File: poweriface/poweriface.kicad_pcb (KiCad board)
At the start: 2 copper layers, 25 x 42.5 mm, 21 parts, among them J1 Power Board, J2 CAN In, J3 CAN Out, J4 AVR-ISP-6, U1 ATmega32M1-AU, U2 MCP2551-I-SN, Y1 16MHz

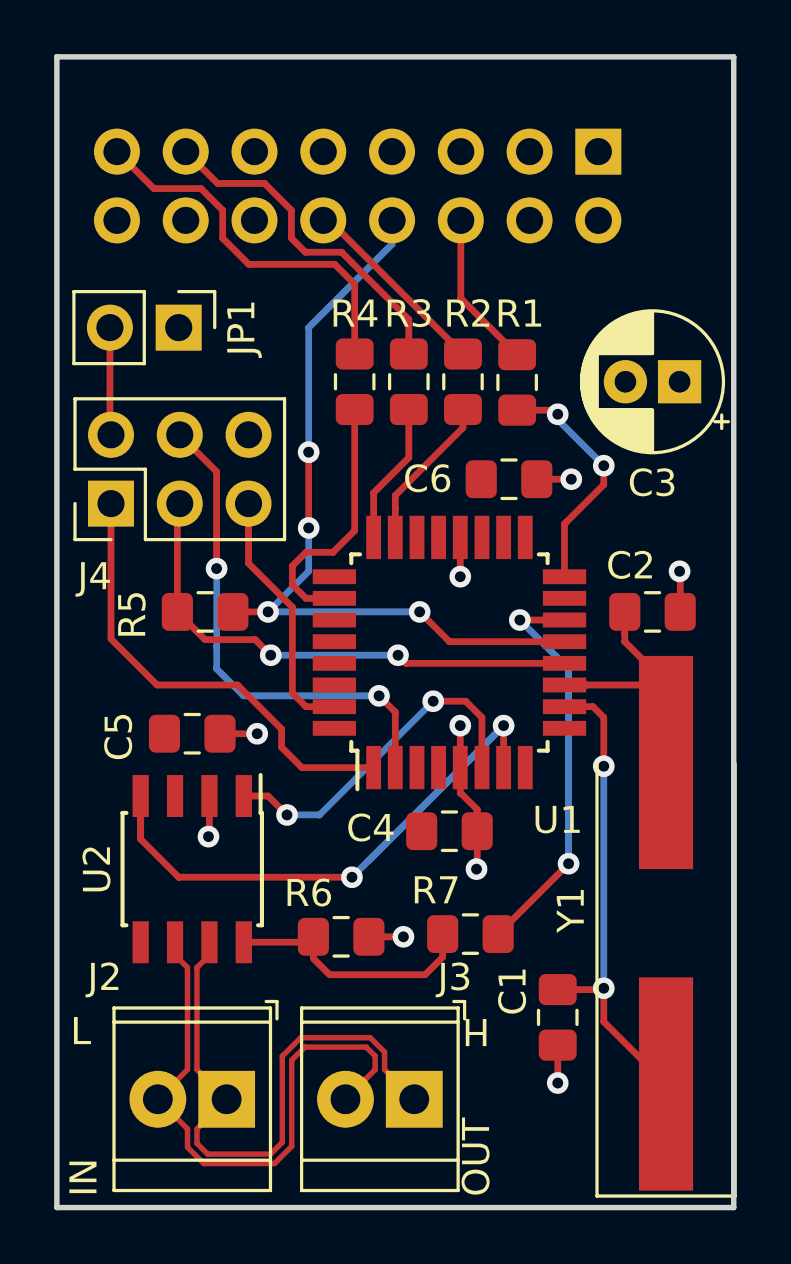
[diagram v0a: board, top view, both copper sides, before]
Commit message: Replaced crystal footprint with less wasteful one
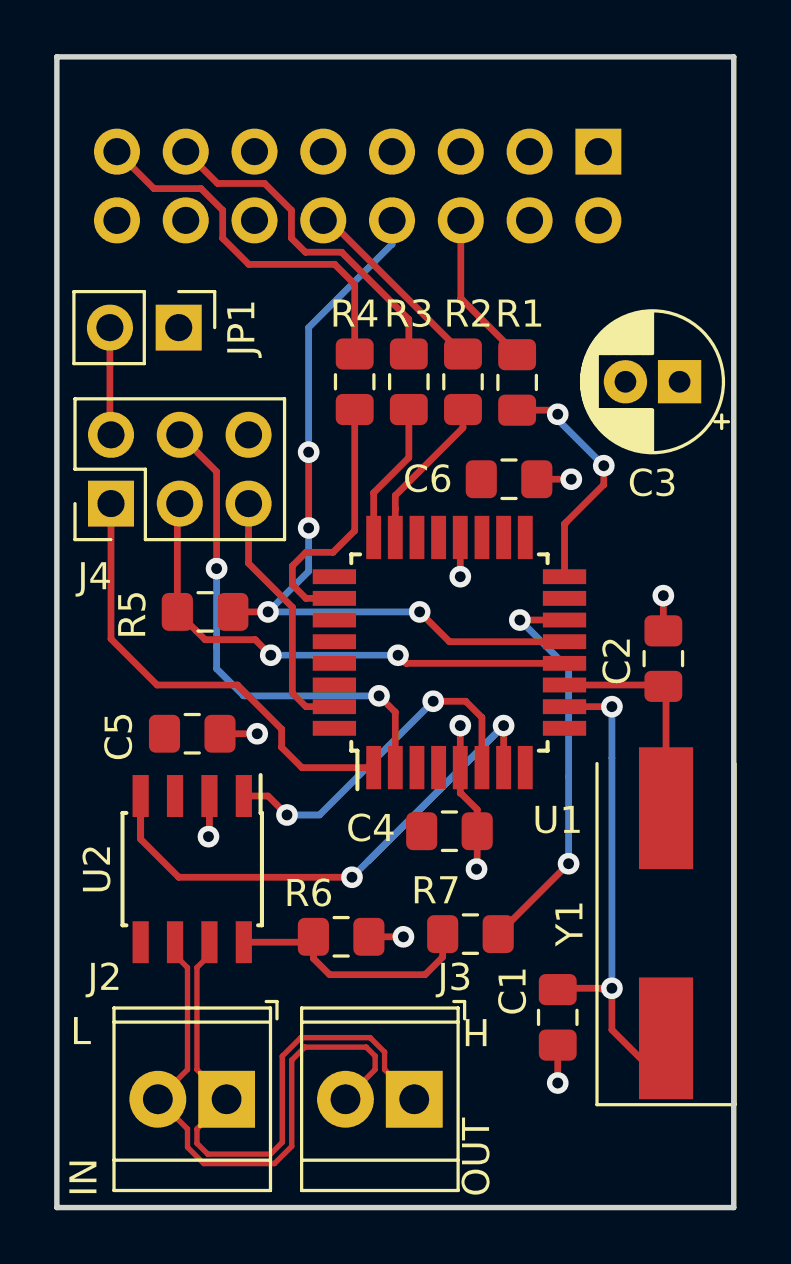
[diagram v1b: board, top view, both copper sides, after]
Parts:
- Y1: footprint Crystal:Crystal_SMD_HC49-SD_HandSoldering -> Crystal:Crystal_SMD_HC49-SD
- moved C2 1.77 mm to (192.4, 98.7), turned to 270 degrees
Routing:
- net Net-(C2-Pad2): track 12.6 -> 8.21 mm
- net Net-(C1-Pad2): track 17.8 -> 18.6 mm

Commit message: Added ground terminals
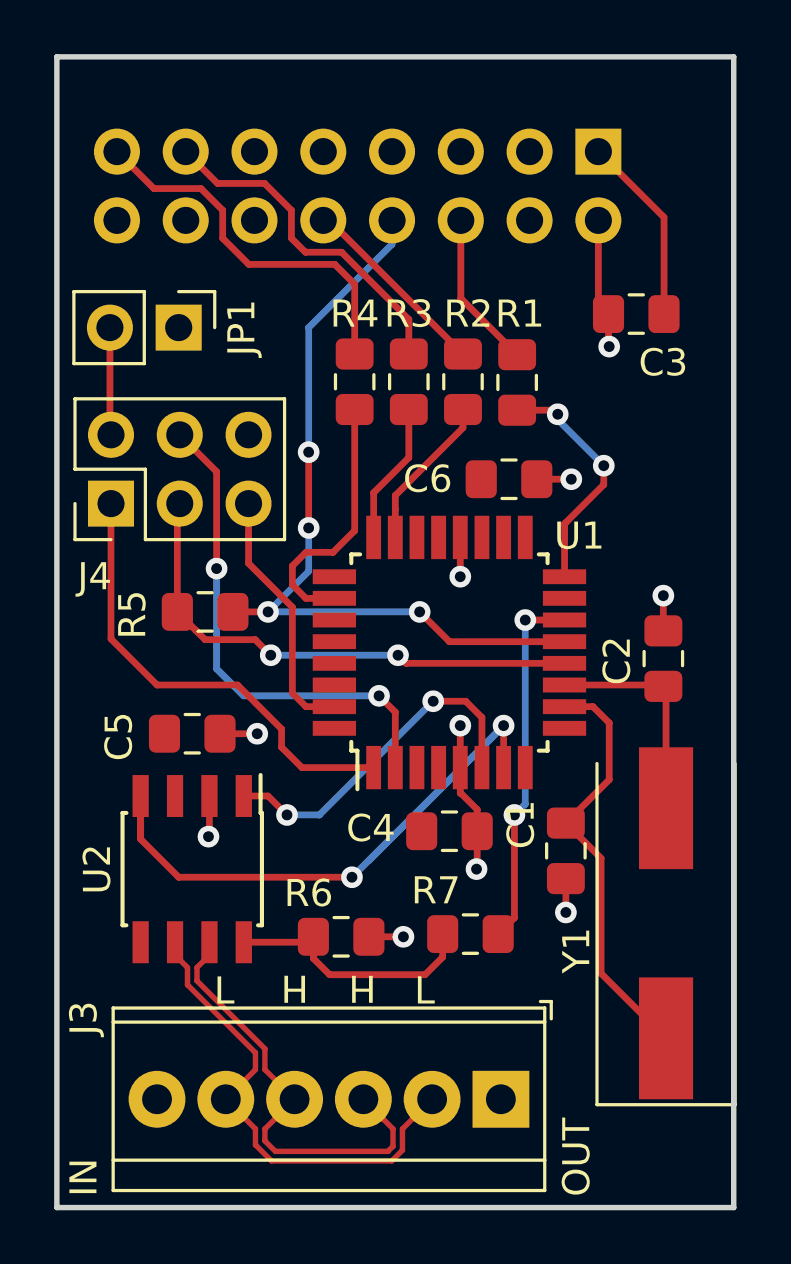
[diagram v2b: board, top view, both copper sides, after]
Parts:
- removed J2: CAN In, TerminalBlock_TE-Connectivity:TerminalBlock_TE_282834-2_1x02_P2.54mm_Horizontal
- C3: footprint Capacitor_THT:CP_Radial_D5.0mm_P2.00mm -> Capacitor_SMD:C_0805_2012Metric_Pad1.15x1.40mm_HandSolder
- J3: value CAN Out -> CAN_SHIELD; footprint TerminalBlock_TE-Connectivity:TerminalBlock_TE_282834-2_1x02_P2.54mm_Horizontal -> TerminalBlock_TE-Connectivity:TerminalBlock_TE_282834-6_1x06_P2.54mm_Horizontal
- R7: value 0 -> DNP
- moved C1 6.16 mm to (188.8, 105.8)
- moved J3 3.20 mm to (186.4, 115.0)
- moved C3 2.97 mm to (191.4, 86.0)
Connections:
- J3 pad 1: /CAN_P -> GND
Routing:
- net +5V: track 0.00 -> 7.00 mm
- net /CAN_P: track 21.7 -> 16.6 mm
- net GND: track 15.2 -> 19.8 mm, vias 9 -> 10
- net /CAN_N: track 21.7 -> 17.8 mm
- net Net-(C1-Pad2): track 18.6 -> 15.7 mm, vias 2 -> 0
- net /HISPEED: track 15.1 -> 13.5 mm

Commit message: poweriface: improve labeling
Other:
- board text added: "⏚ L H H L ⏚"
- board text removed: "H"
- board text removed: "L"
